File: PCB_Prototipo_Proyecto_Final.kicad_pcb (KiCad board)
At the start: 2 copper layers, 165.1 x 154.9 mm, 126 parts, among them IC1 MCP6486T-E_OT, J1 VIN, J10 Terminal_Sensores_Nivel, J11 Terminal_Sensor_Flujo, J12 Rele_4, J13 Rele_7, J14 Rele_1, J15 Rele_5, J16 Rele_2, J17 Rele_3, J18 Rele_6, J2 Conn_01x15, J3 Conn_01x15, J4 Terminal_Sensor_pH, J5 Terminal_Sensor_CO2, J6 Terminal_Sensor_TDS, J7 Terminal_Sensor_Temp_Sumerg, J8 Terminal_Sensor_Iluminacion, J9 Terminal_Sensor_Temp_y_Hum, K1 SRD-05VDC-SL-C, K2 SRD-05VDC-SL-C, K3 SRD-05VDC-SL-C, K4 SRD-05VDC-SL-C, K5 SRD-05VDC-SL-C, K6 SRD-05VDC-SL-C, K7 SRD-05VDC-SL-C, Q1 2N7002, Q10 PMBT3904,235, Q11 PMBT3904,235, Q12 PMBT3904,235, Q13 PMBT3904,235, Q14 PMBT3904,235, Q15 PMBT3904,235, Q2 2N7002, Q3 2N7002, Q4 2N7002, Q5 2N7002, Q6 2N7002, Q7 2N7002, Q8 2N7002, Q9 PMBT3904,235, U1 LM2596S-5, U2 LM1117-3.3, U3 MCP23008-xP

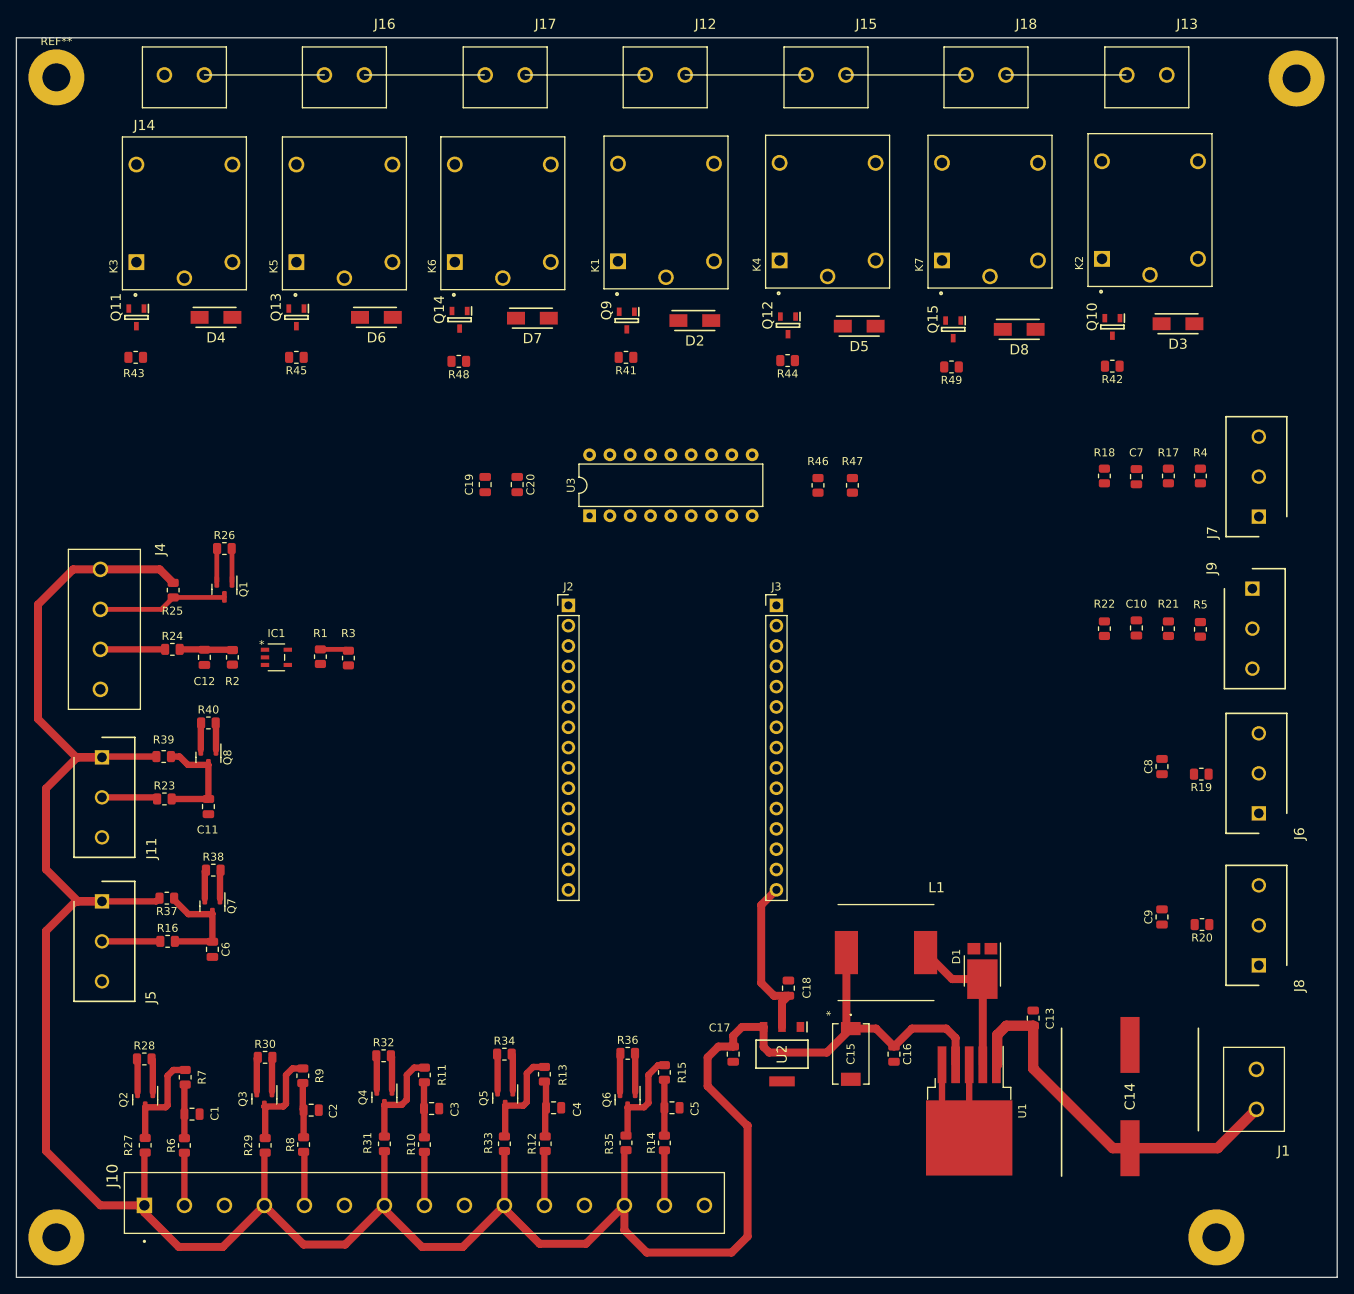
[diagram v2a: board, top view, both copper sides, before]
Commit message: Se finalizó con el PCB del prototipo.
Dado que se buscó a toda costa que el PCB fuera de 1 capa, en varios puntos del circuito se tuvieron que agregar pin headers individuales para conectar a 3V3 y GND, junto con tiras de pin headers. Cada una de estas se conectara luego entre si mediante cables.

Tambien se generaron los archivos Gerber y BOM.
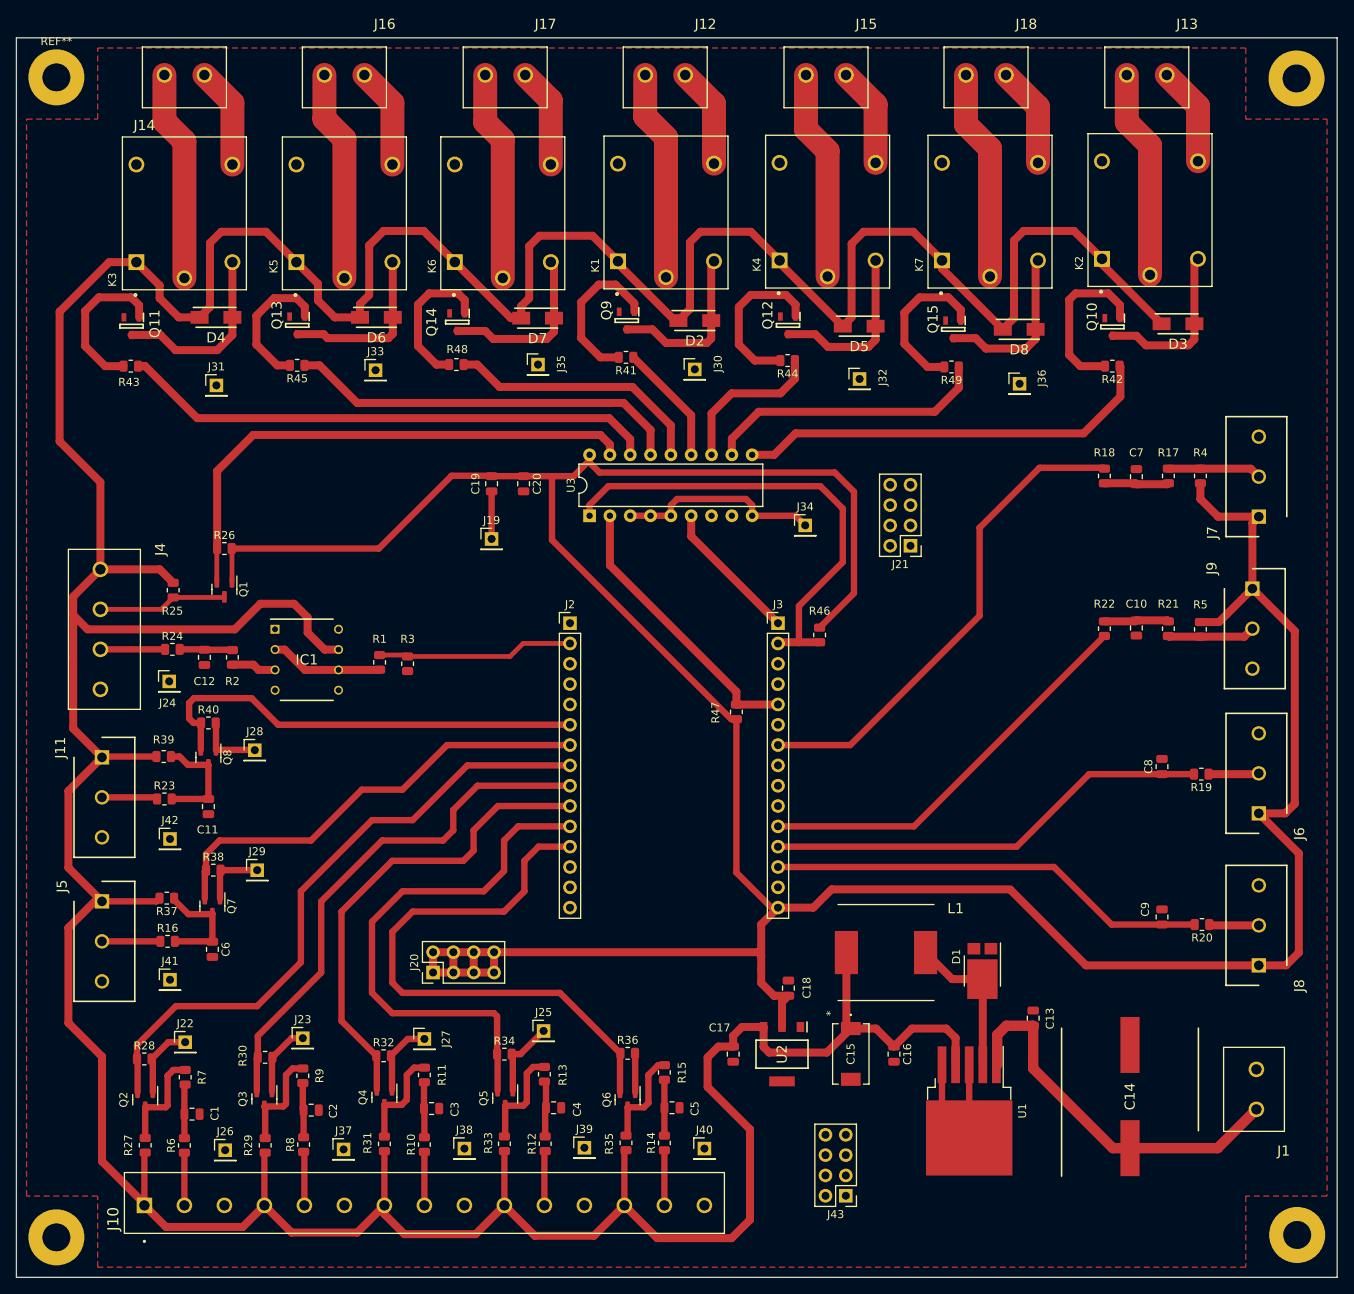
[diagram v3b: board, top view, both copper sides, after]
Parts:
- added J19: Pin GND, Connector_PinHeader_2.54mm:PinHeader_1x01_P2.54mm_Vertical, F.Cu at (196.6, 116.0)
- added J20: Conector 3V3, Connector_PinHeader_2.54mm:PinHeader_2x04_P2.54mm_Vertical, F.Cu at (189.2, 170.2)
- added J21: Conector GND, Connector_PinHeader_2.54mm:PinHeader_2x04_P2.54mm_Vertical, F.Cu at (248.9, 116.8)
- added J22: Pin_3V3, Connector_PinHeader_2.54mm:PinHeader_1x01_P2.54mm_Vertical, F.Cu at (158.3, 178.9)
- added J23: Pin_3V3, Connector_PinHeader_2.54mm:PinHeader_1x01_P2.54mm_Vertical, F.Cu at (173.0, 178.4)
- added J24: Pin GND, Connector_PinHeader_2.54mm:PinHeader_1x01_P2.54mm_Vertical, F.Cu at (156.3, 133.8)
- added J25: Pin_3V3, Connector_PinHeader_2.54mm:PinHeader_1x01_P2.54mm_Vertical, F.Cu at (203.1, 177.5)
- added J26: Pin GND, Connector_PinHeader_2.54mm:PinHeader_1x01_P2.54mm_Vertical, F.Cu at (163.3, 192.4)
- added J27: Pin_3V3, Connector_PinHeader_2.54mm:PinHeader_1x01_P2.54mm_Vertical, F.Cu at (188.2, 178.5)
- added J28: Pin_3V3, Connector_PinHeader_2.54mm:PinHeader_1x01_P2.54mm_Vertical, F.Cu at (167.0, 142.4)
- added J29: Pin_3V3, Connector_PinHeader_2.54mm:PinHeader_1x01_P2.54mm_Vertical, F.Cu at (167.3, 157.4)
- added J30: Pin GND, Connector_PinHeader_2.54mm:PinHeader_1x01_P2.54mm_Vertical, F.Cu at (222.0, 94.8)
- added J31: Pin GND, Connector_PinHeader_2.54mm:PinHeader_1x01_P2.54mm_Vertical, F.Cu at (162.2, 96.8)
- added J32: Pin GND, Connector_PinHeader_2.54mm:PinHeader_1x01_P2.54mm_Vertical, F.Cu at (242.6, 96.0)
- added J33: Pin GND, Connector_PinHeader_2.54mm:PinHeader_1x01_P2.54mm_Vertical, F.Cu at (182.1, 94.9)
- added J34: Pin GND, Connector_PinHeader_2.54mm:PinHeader_1x01_P2.54mm_Vertical, F.Cu at (235.8, 114.3)
- added J35: Pin GND, Connector_PinHeader_2.54mm:PinHeader_1x01_P2.54mm_Vertical, F.Cu at (202.4, 94.2)
- added J36: Pin GND, Connector_PinHeader_2.54mm:PinHeader_1x01_P2.54mm_Vertical, F.Cu at (262.6, 96.6)
- added J37: Pin GND, Connector_PinHeader_2.54mm:PinHeader_1x01_P2.54mm_Vertical, F.Cu at (178.1, 192.3)
- added J38: Pin GND, Connector_PinHeader_2.54mm:PinHeader_1x01_P2.54mm_Vertical, F.Cu at (193.2, 192.2)
- added J39: Pin GND, Connector_PinHeader_2.54mm:PinHeader_1x01_P2.54mm_Vertical, F.Cu at (208.2, 192.1)
- added J40: Pin GND, Connector_PinHeader_2.54mm:PinHeader_1x01_P2.54mm_Vertical, F.Cu at (223.2, 192.2)
- added J41: Pin GND, Connector_PinHeader_2.54mm:PinHeader_1x01_P2.54mm_Vertical, F.Cu at (156.4, 171.1)
- added J42: Pin GND, Connector_PinHeader_2.54mm:PinHeader_1x01_P2.54mm_Vertical, F.Cu at (156.4, 153.5)
- added J43: Conector GND, Connector_PinHeader_2.54mm:PinHeader_2x04_P2.54mm_Vertical, F.Cu at (240.8, 198.1)
- IC1: value MCP6486T-E_OT -> UA741CP; footprint MCP6486T-E_OT:MCP6486RT-E&slash_OT -> UA741CP:DIP794W53P254L959H508Q8N
- moved R47 31.8 mm to (227.2, 137.6), turned to 90 degrees
- moved R46 18.7 mm to (237.6, 128.0)
- moved ? 10.1 mm to (297.3, 203.0)
- moved R1 7.43 mm to (182.6, 131.4)
- moved R3 7.43 mm to (186.1, 131.6)
- moved IC1 3.81 mm to (173.5, 131.1)
- moved J2 2.23 mm to (206.4, 126.5)
- moved J3 2.23 mm to (232.4, 126.5)
- moved Q11 1.26 mm to (151.5, 89.4)
- moved R43 1.26 mm to (151.5, 94.4)
- moved Q13 1.00 mm to (172.3, 89.3)
- moved R45 1.00 mm to (172.3, 94.3)
- moved C19 0.81 mm to (196.6, 109.1)
- moved C20 0.81 mm to (200.6, 109.1)
- moved D7 0.65 mm to (202.3, 88.4)
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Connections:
- D2 pad 1: /Salidas/+5V -> +5V
- D3 pad 1: /Salidas/+5V -> +5V
- D4 pad 1: /Salidas/+5V -> +5V
- D5 pad 1: /Salidas/+5V -> +5V
- D6 pad 1: /Salidas/+5V -> +5V
- D7 pad 1: /Salidas/+5V -> +5V
- D8 pad 1: /Salidas/+5V -> +5V
- IC1 pad 1: Net-(IC1-Pad1) -> unconnected-(IC1-Pad1)
- IC1 pad 2: GND -> Net-(IC1-Pad2)
- IC1 pad 4: Net-(IC1-Pad1) -> GND
- IC1 pad 5: +5V -> unconnected-(IC1-Pad5)
- K1 pad A1: /Salidas/+5V -> +5V
- K2 pad A1: /Salidas/+5V -> +5V
- K3 pad A1: /Salidas/+5V -> +5V
- K4 pad A1: /Salidas/+5V -> +5V
- K5 pad A1: /Salidas/+5V -> +5V
- K6 pad A1: /Salidas/+5V -> +5V
- K7 pad A1: /Salidas/+5V -> +5V
- R1 pad 1: Net-(IC1-Pad1) -> Net-(IC1-Pad2)
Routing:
- net +3.3V: track 54.2 -> 463.3 mm
- net +5V: track 345.8 -> 620.9 mm
- net /Microcontrolador/SensorNivel_1: track 4.19 -> 79.7 mm
- net /Microcontrolador/SensorNivel_5: track 4.88 -> 72.3 mm
- net /Microcontrolador/Rele_1: track 0.00 -> 67.2 mm
- net /Microcontrolador/Trigger__pH: track 4.18 -> 66.6 mm
- net /Microcontrolador/SensorNivel_4: track 4.59 -> 67.0 mm
- net /Entradas/Data_SensorTempSumerg: track 0.00 -> 61.6 mm
- net /Microcontrolador/SensorNivel_2: track 4.31 -> 65.7 mm
- net /Microcontrolador/MCP23008_SCL: track 0.00 -> 59.4 mm
- net /Entradas/TDS_Analog: track 0.00 -> 55.8 mm
- net /Microcontrolador/SensorNivel_3: track 4.29 -> 59.6 mm
- net /Entradas/Ilum_Analog: track 0.00 -> 55.1 mm
- net /Microcontrolador/SensorCO2: track 3.62 -> 56.8 mm
- net /Microcontrolador/SensorFlujo: track 3.38 -> 56.3 mm
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- added copper zone on F.Cu, net GND

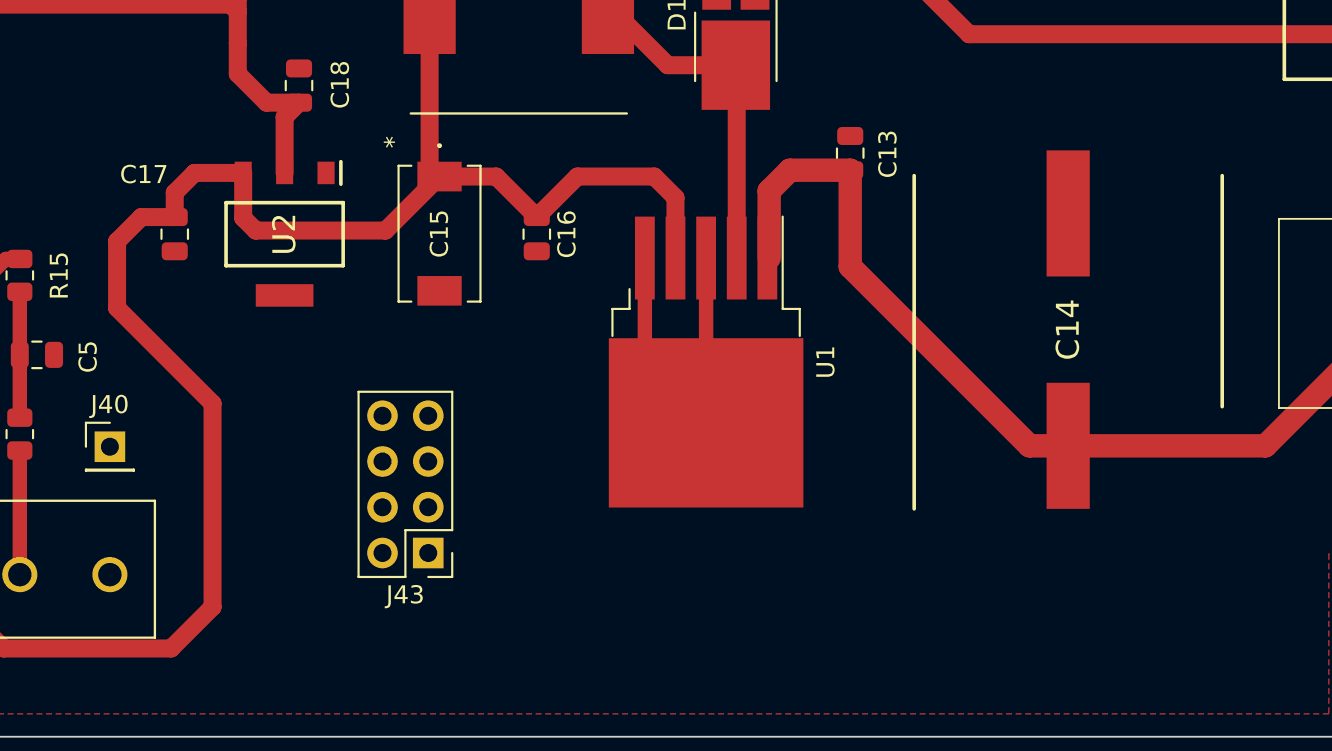
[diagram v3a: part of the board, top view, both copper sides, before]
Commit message: Se modificaron los footprints del capacitor de 470 uF y del LM1117.
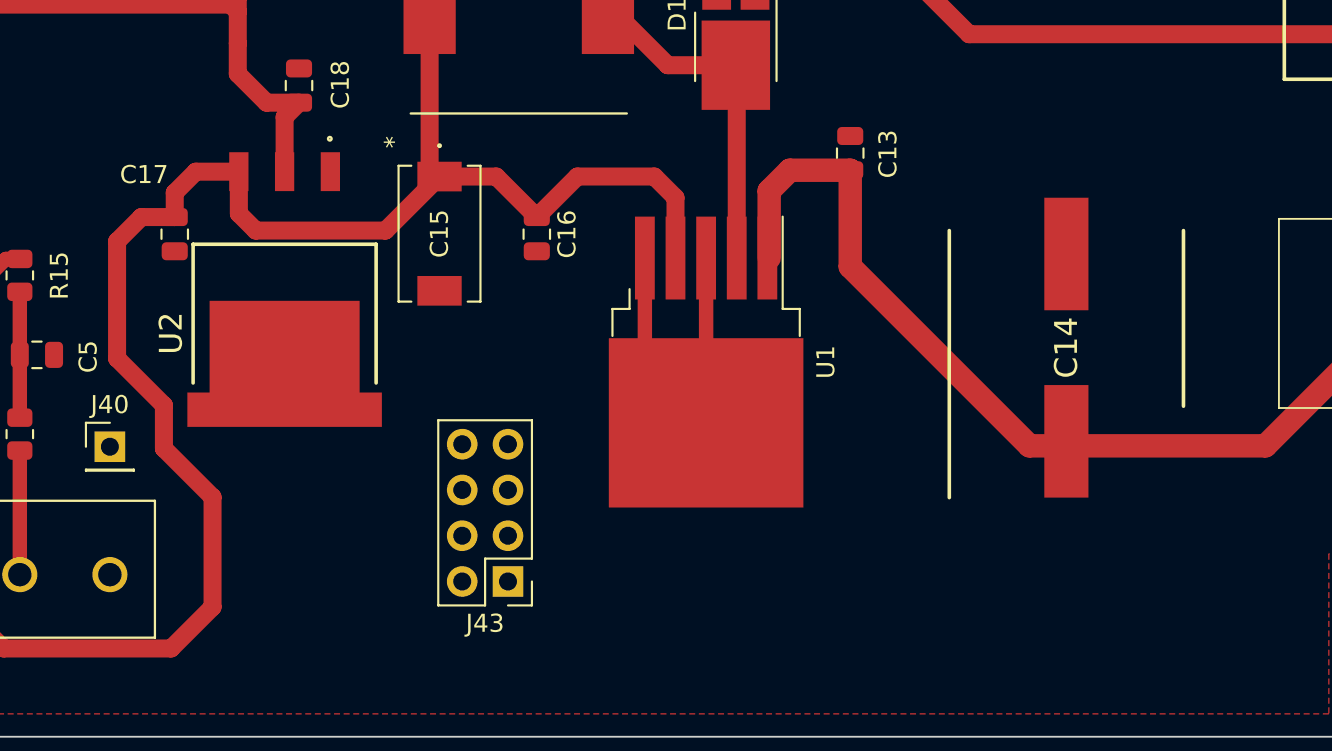
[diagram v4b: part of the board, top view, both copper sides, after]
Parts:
- C14: footprint UUG1H471MNQ6MS:CAPAE1710X1750N -> VE-471M1HTR-1316:CAPAE1300X1650N
- U2: footprint LM1117MPX-33NOPB:SOT230P700X180-4N -> LM1117SX-3V3-NOPB:KTT0003B
- moved U2 9.20 mm to (232.9, 189.6), turned to 90 degrees
- moved J43 4.70 mm to (245.3, 199.7)
- moved C14 1.00 mm to (276.3, 186.7)
